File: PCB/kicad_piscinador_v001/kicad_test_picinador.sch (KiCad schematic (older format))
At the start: 2 parts, among them U1 DG441, U2 DG441

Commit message: bk pcb
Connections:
- wire segments 18 -> 22
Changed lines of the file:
@@
 Wire Wire Line
 	2750 3700 3050 3700
+Wire Wire Line
+	3350 3850 3350 3950
+Wire Wire Line
+	3350 3950 2800 3950
+Wire Wire Line
+	2800 3950 2800 3850
+Wire Wire Line
+	2800 3850 3050 3850
 $EndSCHEMATC

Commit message: PCB ----------------- Update
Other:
- moved on the sheet: U1A, U2A, U2B, U2C, U2D
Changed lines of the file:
@@
 L DG441 U1
 U 1 1 57F7D239
-P 3400 2150
-F 0 "U1" H 3600 2005 50  0000 C CNN
-F 1 "DG441" H 3600 2300 50  0000 C CNN
-F 2 "soic:SOIC-16" H 3400 2150 60  0001 C CNN
-F 3 "" H 3400 2150 60  0001 C CNN
-	1    3400 2150
+P 5700 1500
+F 0 "U1" H 5900 1355 50  0000 C CNN
+F 1 "DG441" H 5900 1650 50  0000 C CNN
+F 2 "soic:SOIC-16" H 5700 1500 60  0001 C CNN
+F 3 "" H 5700 1500 60  0001 C CNN
+	1    5700 1500
 	1    0    0    -1
 $EndComp
@@
 L DG441 U2
 U 3 1 57F7D2A5
-P 3400 2650
-F 0 "U2" H 3600 2505 50  0000 C CNN
-F 1 "DG441" H 3600 2800 50  0000 C CNN
-F 2 "soic:SOIC-16" H 3400 2650 60  0001 C CNN
-F 3 "" H 3400 2650 60  0001 C CNN
-	3    3400 2650
+P 5700 2000
+F 0 "U2" H 5900 1855 50  0000 C CNN
+F 1 "DG441" H 5900 2150 50  0000 C CNN
+F 2 "soic:SOIC-16" H 5700 2000 60  0001 C CNN
+F 3 "" H 5700 2000 60  0001 C CNN
+	3    5700 2000
 	1    0    0    -1
 $EndComp
@@
 L DG441 U2
 U 1 1 57F7D2FA
-P 3350 3200
-F 0 "U2" H 3550 3055 50  0000 C CNN
-F 1 "DG441" H 3550 3350 50  0000 C CNN
-F 2 "soic:SOIC-16" H 3350 3200 60  0001 C CNN
-F 3 "" H 3350 3200 60  0001 C CNN
-	1    3350 3200
+P 5650 2550
+F 0 "U2" H 5850 2405 50  0000 C CNN
+F 1 "DG441" H 5850 2700 50  0000 C CNN
+F 2 "soic:SOIC-16" H 5650 2550 60  0001 C CNN
+F 3 "" H 5650 2550 60  0001 C CNN
+	1    5650 2550
 	1    0    0    -1
 $EndComp
@@
 L DG441 U2
 U 2 1 57F7D33F
-P 3350 3700
-F 0 "U2" H 3550 3555 50  0000 C CNN
-F 1 "DG441" H 3550 3850 50  0000 C CNN
-F 2 "soic:SOIC-16" H 3350 3700 60  0001 C CNN
-F 3 "" H 3350 3700 60  0001 C CNN
-	2    3350 3700
+P 5650 3050
+F 0 "U2" H 5850 2905 50  0000 C CNN
+F 1 "DG441" H 5850 3200 50  0000 C CNN
+F 2 "soic:SOIC-16" H 5650 3050 60  0001 C CNN
+F 3 "" H 5650 3050 60  0001 C CNN
+	2    5650 3050
 	1    0    0    -1
 $EndComp
 Wire Wire Line
-	3700 2150 4200 2150
+	6000 1500 6500 1500
 Wire Wire Line
-	4200 2150 4200 2700
+	6500 1500 6500 2050
 Wire Wire Line
-	4200 2700 3700 2700
+	6500 2050 6000 2050
 Wire Wire Line
-	3700 2700 3700 2650
+	6000 2050 6000 2000
 $Comp
 L DG441 U2
 U 4 1 57F7E884
-P 4450 3300
-F 0 "U2" H 4650 3155 50  0000 C CNN
-F 1 "DG441" H 4650 3450 50  0000 C CNN
-F 2 "soic:SOIC-16" H 4450 3300 60  0001 C CNN
-F 3 "" H 4450 3300 60  0001 C CNN
-	4    4450 3300
+P 6750 2650
+F 0 "U2" H 6950 2505 50  0000 C CNN
+F 1 "DG441" H 6950 2800 50  0000 C CNN
+F 2 "soic:SOIC-16" H 6750 2650 60  0001 C CNN
+F 3 "" H 6750 2650 60  0001 C CNN
+	4    6750 2650
 	1    0    0    -1
 $EndComp
 Wire Wire Line
-	4150 3300 4150 3200
+	6450 2650 6450 2550
 Wire Wire Line
-	4150 3200 3650 3200
+	6450 2550 5950 2550
 Wire Wire Line
-	4150 3450 3650 3450
+	6450 2800 5950 2800
 Wire Wire Line
-	3650 3450 3650 3700
+	5950 2800 5950 3050
 Wire Wire Line
-	4750 3300 3050 3300
+	7050 2650 5350 2650
 Wire Wire Line
-	3050 3300 3050 3700
+	5350 2650 5350 3050
 $Sheet
-S 5050 2700 1150 850
+S 1000 900  950  400
 U 57F8A4BF
 F0 "BatteryCharger" 60
@@
 $EndSheet
 Wire Wire Line
-	3400 1900 3400 2150
+	5700 1250 5700 1500
 Wire Wire Line
-	3400 2150 3100 2150
+	5700 1500 5400 1500
 Wire Wire Line
-	3200 2100 3000 2100
+	5500 1450 5300 1450
 Wire Wire Line
-	3000 2100 3000 2300
+	5300 1450 5300 1650
 Wire Wire Line
-	3000 2300 3100 2300
+	5300 1650 5400 1650
 Wire Wire Line
-	3100 2650 2750 2650
+	5400 2000 5050 2000
 Wire Wire Line
-	2750 2650 2750 3700
+	5050 2000 5050 3050
 Wire Wire Line
-	2750 3700 3050 3700
+	5050 3050 5350 3050
 Wire Wire Line
-	3350 3850 3350 3950
+	5650 3200 5650 3300
 Wire Wire Line
-	3350 3950 2800 3950
+	5650 3300 5100 3300
 Wire Wire Line
-	2800 3950 2800 3850
+	5100 3300 5100 3200
 Wire Wire Line
-	2800 3850 3050 3850
+	5100 3200 5350 3200
 $EndSCHEMATC

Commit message: pcb project
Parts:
- removed unit 3 of U2
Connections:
- wire segments 22 -> 14
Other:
- moved on the sheet: U1A, U2A, U2B, U2D
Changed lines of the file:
@@
 LIBS:valves
 LIBS:Zilog
+LIBS:Common-Parts-Library
 LIBS:kicad_test_picinador-cache
 EELAYER 25 0
@@
 L DG441 U1
 U 1 1 57F7D239
-P 5700 1500
-F 0 "U1" H 5900 1355 50  0000 C CNN
-F 1 "DG441" H 5900 1650 50  0000 C CNN
-F 2 "soic:SOIC-16" H 5700 1500 60  0001 C CNN
-F 3 "" H 5700 1500 60  0001 C CNN
-	1    5700 1500
-	1    0    0    -1
-$EndComp
-$Comp
-L DG441 U2
-U 3 1 57F7D2A5
-P 5700 2000
-F 0 "U2" H 5900 1855 50  0000 C CNN
-F 1 "DG441" H 5900 2150 50  0000 C CNN
-F 2 "soic:SOIC-16" H 5700 2000 60  0001 C CNN
-F 3 "" H 5700 2000 60  0001 C CNN
-	3    5700 2000
+P 5600 1500
+F 0 "U1" H 5800 1355 50  0000 C CNN
+F 1 "DG441" H 5800 1650 50  0000 C CNN
+F 2 "soic:SOIC-16" H 5600 1500 60  0001 C CNN
+F 3 "" H 5600 1500 60  0001 C CNN
+	1    5600 1500
 	1    0    0    -1
 $EndComp
@@
 L DG441 U2
 U 1 1 57F7D2FA
-P 5650 2550
-F 0 "U2" H 5850 2405 50  0000 C CNN
-F 1 "DG441" H 5850 2700 50  0000 C CNN
-F 2 "soic:SOIC-16" H 5650 2550 60  0001 C CNN
-F 3 "" H 5650 2550 60  0001 C CNN
-	1    5650 2550
+P 5600 2000
+F 0 "U2" H 5800 1855 50  0000 C CNN
+F 1 "DG441" H 5800 2150 50  0000 C CNN
+F 2 "soic:SOIC-16" H 5600 2000 60  0001 C CNN
+F 3 "" H 5600 2000 60  0001 C CNN
+	1    5600 2000
 	1    0    0    -1
 $EndComp
@@
 L DG441 U2
 U 2 1 57F7D33F
-P 5650 3050
-F 0 "U2" H 5850 2905 50  0000 C CNN
-F 1 "DG441" H 5850 3200 50  0000 C CNN
-F 2 "soic:SOIC-16" H 5650 3050 60  0001 C CNN
-F 3 "" H 5650 3050 60  0001 C CNN
-	2    5650 3050
+P 5500 3400
+F 0 "U2" H 5700 3255 50  0000 C CNN
+F 1 "DG441" H 5700 3550 50  0000 C CNN
+F 2 "soic:SOIC-16" H 5500 3400 60  0001 C CNN
+F 3 "" H 5500 3400 60  0001 C CNN
+	2    5500 3400
 	1    0    0    -1
 $EndComp
 Wire Wire Line
-	6000 1500 6500 1500
+	5250 2750 4950 2750
 Wire Wire Line
-	6500 1500 6500 2050
+	5850 2600 6200 2600
 Wire Wire Line
-	6500 2050 6000 2050
-Wire Wire Line
-	6000 2050 6000 2000
-$Comp
-L DG441 U2
-U 4 1 57F7E884
-P 6750 2650
-F 0 "U2" H 6950 2505 50  0000 C CNN
-F 1 "DG441" H 6950 2800 50  0000 C CNN
-F 2 "soic:SOIC-16" H 6750 2650 60  0001 C CNN
-F 3 "" H 6750 2650 60  0001 C CNN
-	4    6750 2650
-	1    0    0    -1
-$EndComp
-Wire Wire Line
-	6450 2650 6450 2550
-Wire Wire Line
-	6450 2550 5950 2550
-Wire Wire Line
-	6450 2800 5950 2800
-Wire Wire Line
-	5950 2800 5950 3050
-Wire Wire Line
-	7050 2650 5350 2650
-Wire Wire Line
-	5350 2650 5350 3050
+	6200 2600 7150 2600
 $Sheet
 S 1000 900  950  400
@@
 $EndSheet
 Wire Wire Line
-	5700 1250 5700 1500
+	4800 1500 5300 1500
 Wire Wire Line
-	5700 1500 5400 1500
+	4800 1650 5300 1650
+$Comp
+L DG441 U2
+U 4 1 57F7E884
+P 5550 2600
+F 0 "U2" H 5750 2455 50  0000 C CNN
+F 1 "DG441" H 5750 2750 50  0000 C CNN
+F 2 "soic:SOIC-16" H 5550 2600 60  0001 C CNN
+F 3 "" H 5550 2600 60  0001 C CNN
+	4    5550 2600
+	1    0    0    -1
+$EndComp
 Wire Wire Line
-	5500 1450 5300 1450
+	6200 2000 6200 2300
 Wire Wire Line
-	5300 1450 5300 1650
+	6200 2300 5200 2300
 Wire Wire Line
-	5300 1650 5400 1650
+	5200 2300 5200 2600
 Wire Wire Line
-	5400 2000 5050 2000
+	5200 2600 5250 2600
 Wire Wire Line
-	5050 2000 5050 3050
+	5900 2000 6200 2000
 Wire Wire Line
-	5050 3050 5350 3050
+	6200 2600 6200 3050
 Wire Wire Line
-	5650 3200 5650 3300
+	6200 3050 5100 3050
 Wire Wire Line
-	5650 3300 5100 3300
+	5100 3050 5100 3400
+Connection ~ 5100 3400
+Connection ~ 6200 2600
 Wire Wire Line
-	5100 3300 5100 3200
-Wire Wire Line
-	5100 3200 5350 3200
+	5100 3400 5200 3400
 $EndSCHEMATC

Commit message: project backup
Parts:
- added SW?: SW_PUSHBUTTON, symbol SW_PUSHBUTTON
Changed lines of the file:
@@
 LIBS:Zilog
 LIBS:Common-Parts-Library
+LIBS:freetronics_schematic
 LIBS:kicad_test_picinador-cache
 EELAYER 25 0
@@
 	6200 2600 7150 2600
 $Sheet
-S 1000 900  950  400
+S 1250 3150 950  400
 U 57F8A4BF
 F0 "BatteryCharger" 60
 F1 "BatteryCharger.sch" 60
+F2 "V_motor" O R 2200 3300 60
+F3 "V_gnd" O R 2200 3450 60
 $EndSheet
 Wire Wire Line
@@
 Wire Wire Line
 	5100 3400 5200 3400
+$Comp
+L SW_PUSHBUTTON SW?
+U 1 1 57FFC5F9
+P 1600 2250
+F 0 "SW?" H 1450 2360 50  0000 C CNN
+F 1 "SW_PUSHBUTTON" H 1600 2170 50  0000 C CNN
+F 2 "" H 1600 2250 60  0000 C CNN
+F 3 "" H 1600 2250 60  0000 C CNN
+	1    1600 2250
+	1    0    0    -1
+$EndComp
 $EndSCHEMATC

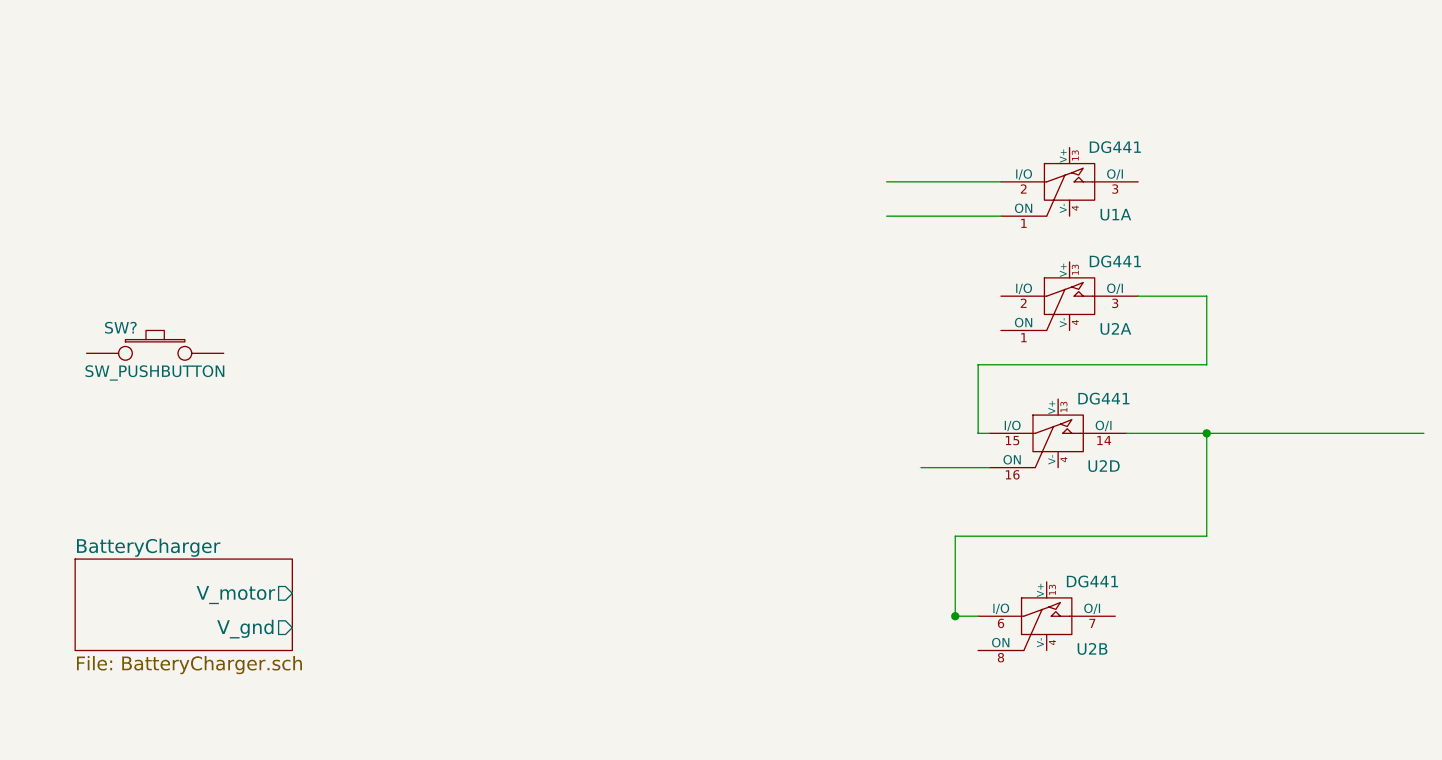
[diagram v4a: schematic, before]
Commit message: Piscinador----------------- Add ltc3121 boost converter
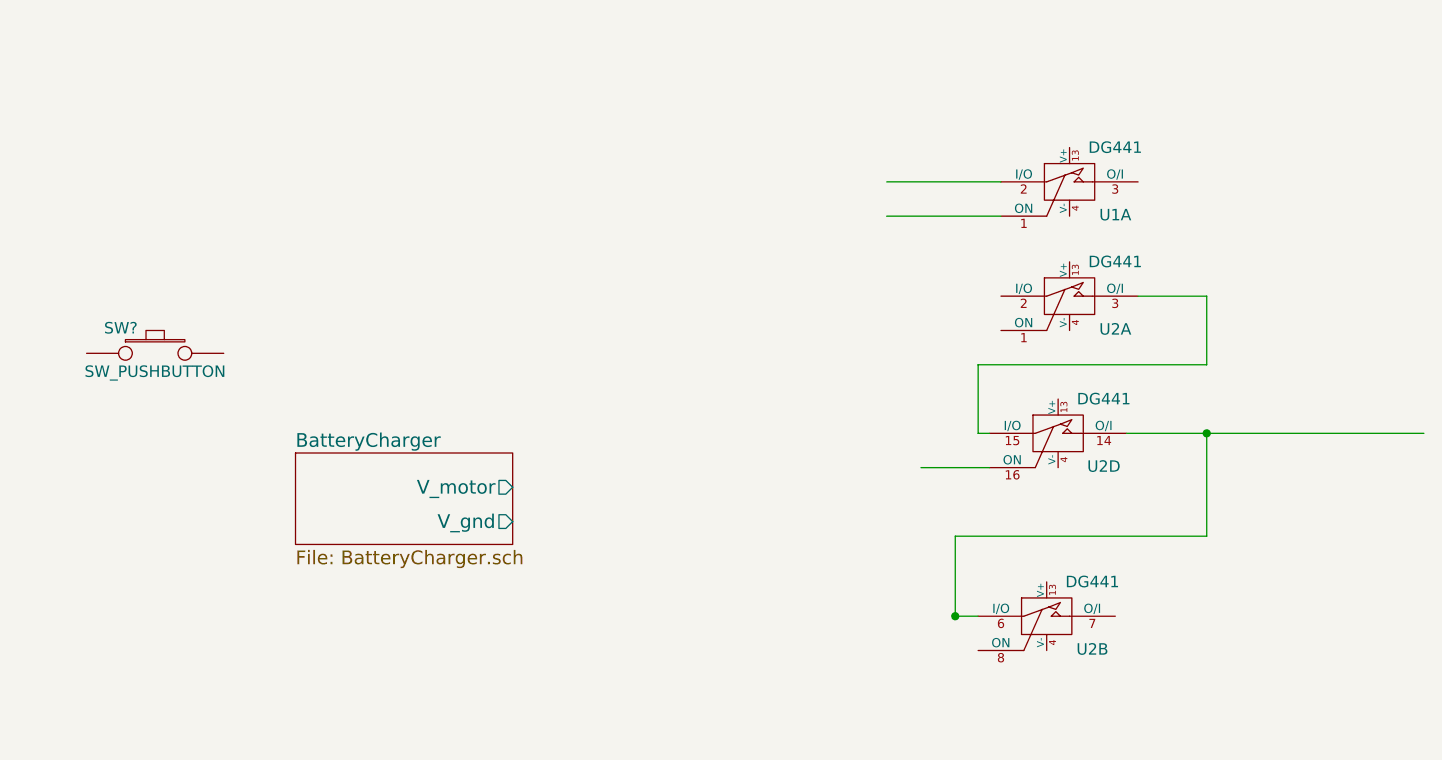
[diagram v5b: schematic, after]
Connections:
- wire segments 14 -> 13
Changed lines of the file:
@@
 LIBS:Zilog
 LIBS:Common-Parts-Library
-LIBS:freetronics_schematic
 LIBS:kicad_test_picinador-cache
 EELAYER 25 0
@@
 	5250 2750 4950 2750
 Wire Wire Line
-	5850 2600 6200 2600
-Wire Wire Line
-	6200 2600 7150 2600
+	5850 2600 7150 2600
 $Sheet
-S 1250 3150 950  400
+S 2214 2686 950  400
 U 57F8A4BF
 F0 "BatteryCharger" 60
 F1 "BatteryCharger.sch" 60
-F2 "V_motor" O R 2200 3300 60
-F3 "V_gnd" O R 2200 3450 60
+F2 "V_motor" O R 3164 2836 60
+F3 "V_gnd" O R 3164 2986 60
 $EndSheet
 Wire Wire Line
